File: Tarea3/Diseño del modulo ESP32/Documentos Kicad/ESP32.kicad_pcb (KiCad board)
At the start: 4 copper layers, 27.9 x 48.2 mm, 34 parts, among them J1 10118192-0002LF, J2 Conn_01x19, J3 Conn_01x19, Q1 S8050, Q2 S8050, SW1 SW_Push_Dual, SW2 SW_Push_Dual, U1 AMS1117-3.3, U2 ESP32-WROOM-32, U4 CP2102N-Axx-xQFN28

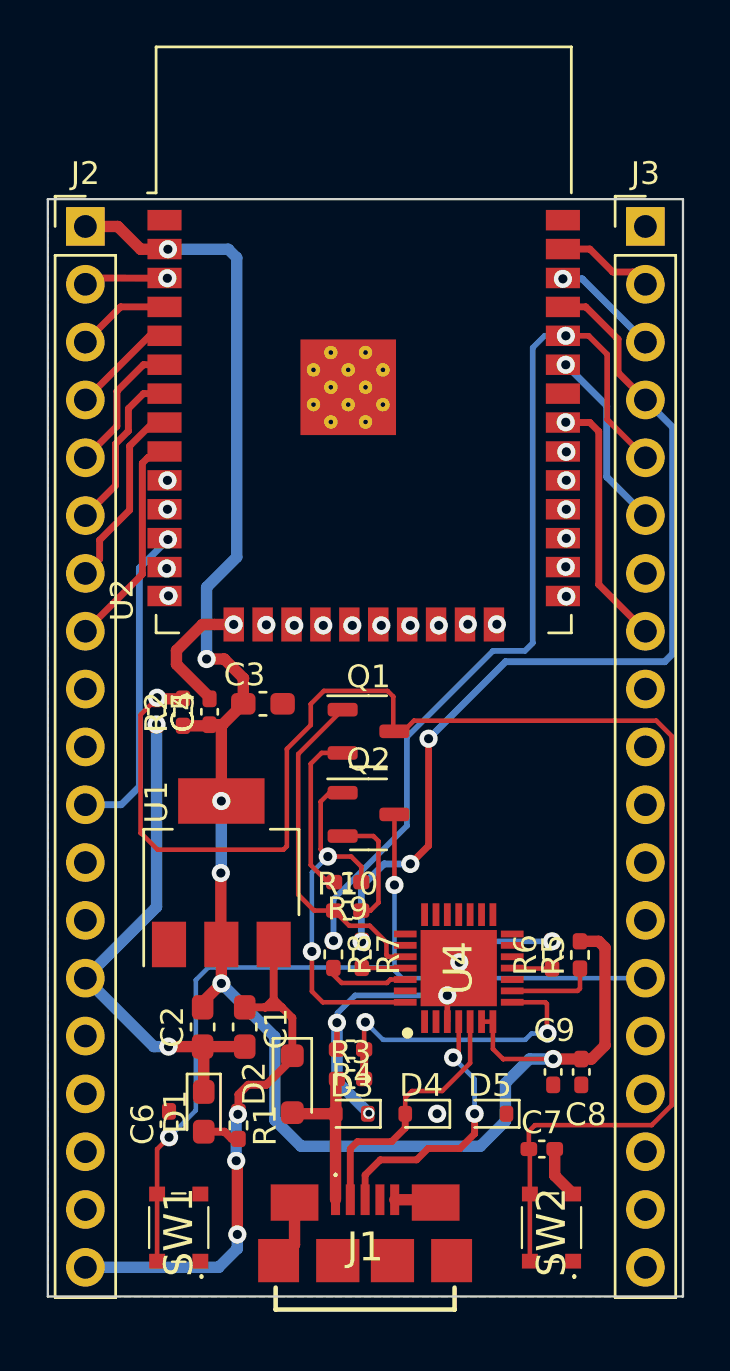
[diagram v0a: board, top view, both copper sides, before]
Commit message: Organizando el F.Mask
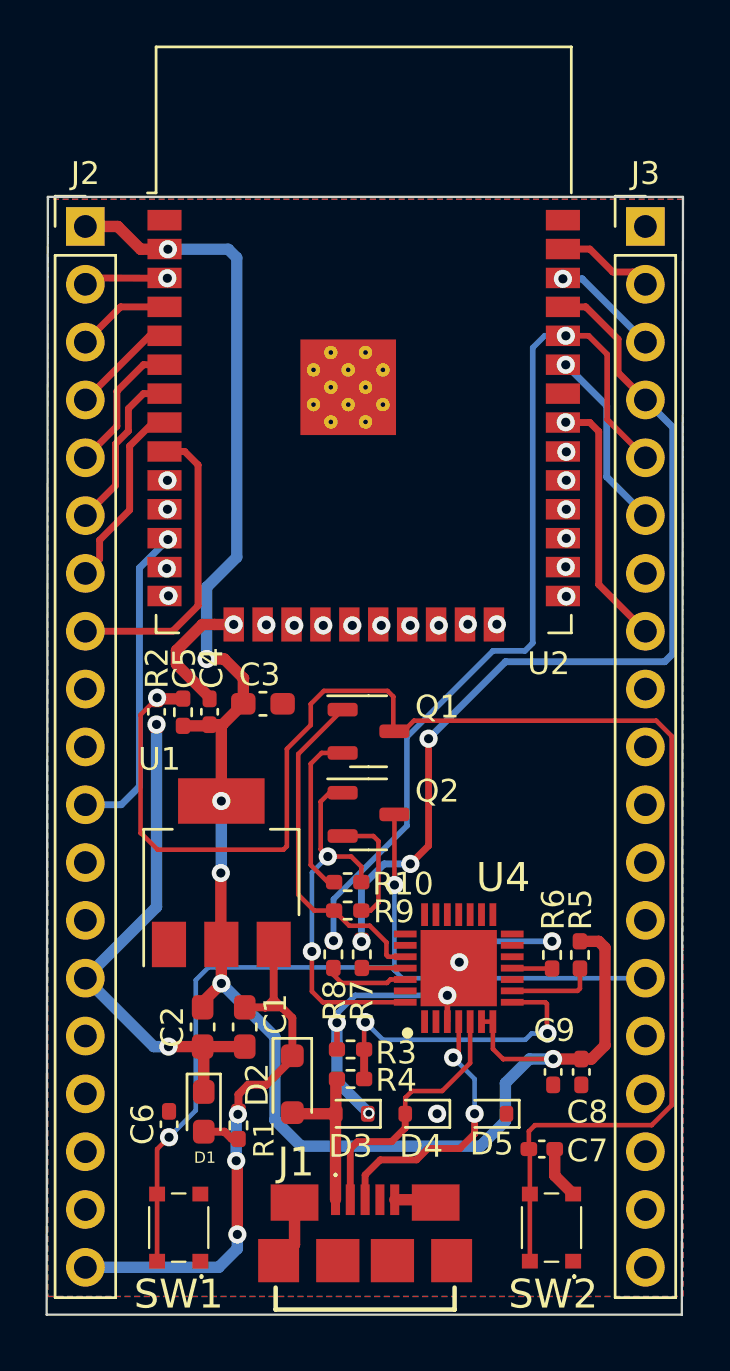
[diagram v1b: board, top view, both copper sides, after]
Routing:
- net /IO33: track 9.73 -> 13.2 mm
- net /EN: track 92.5 -> 93.0 mm
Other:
- board size 27.9 x 48.2 mm -> 28 x 49.1 mm
